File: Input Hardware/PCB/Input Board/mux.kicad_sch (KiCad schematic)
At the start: 4 parts

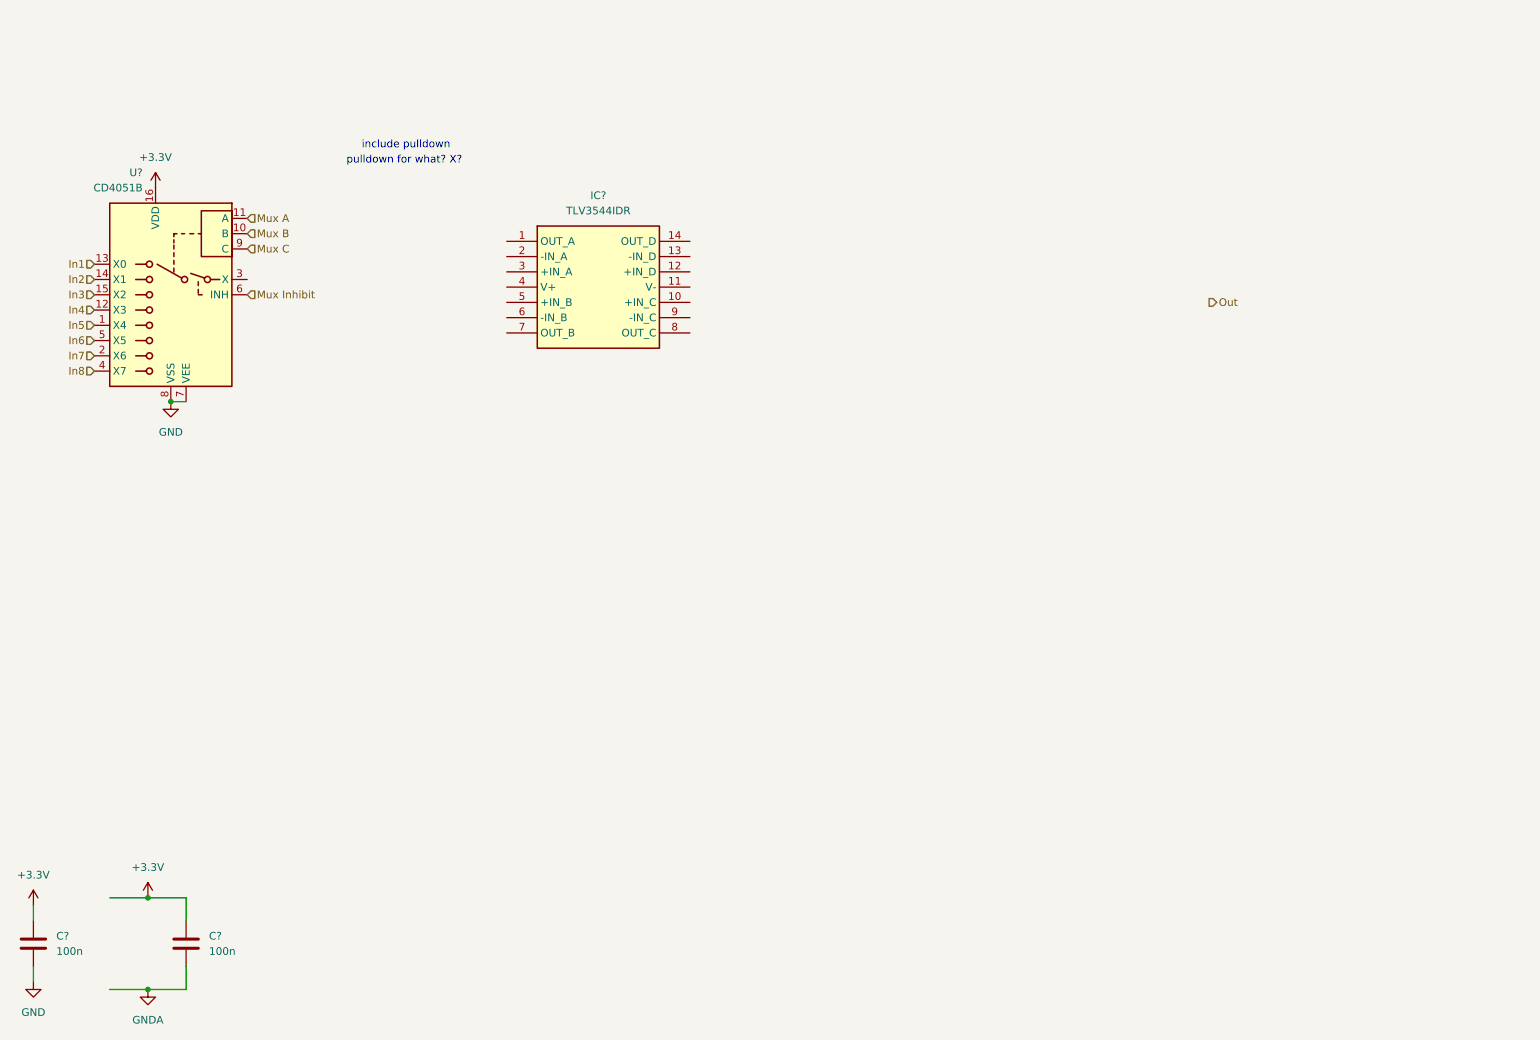
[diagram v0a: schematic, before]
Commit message: opamp symbol
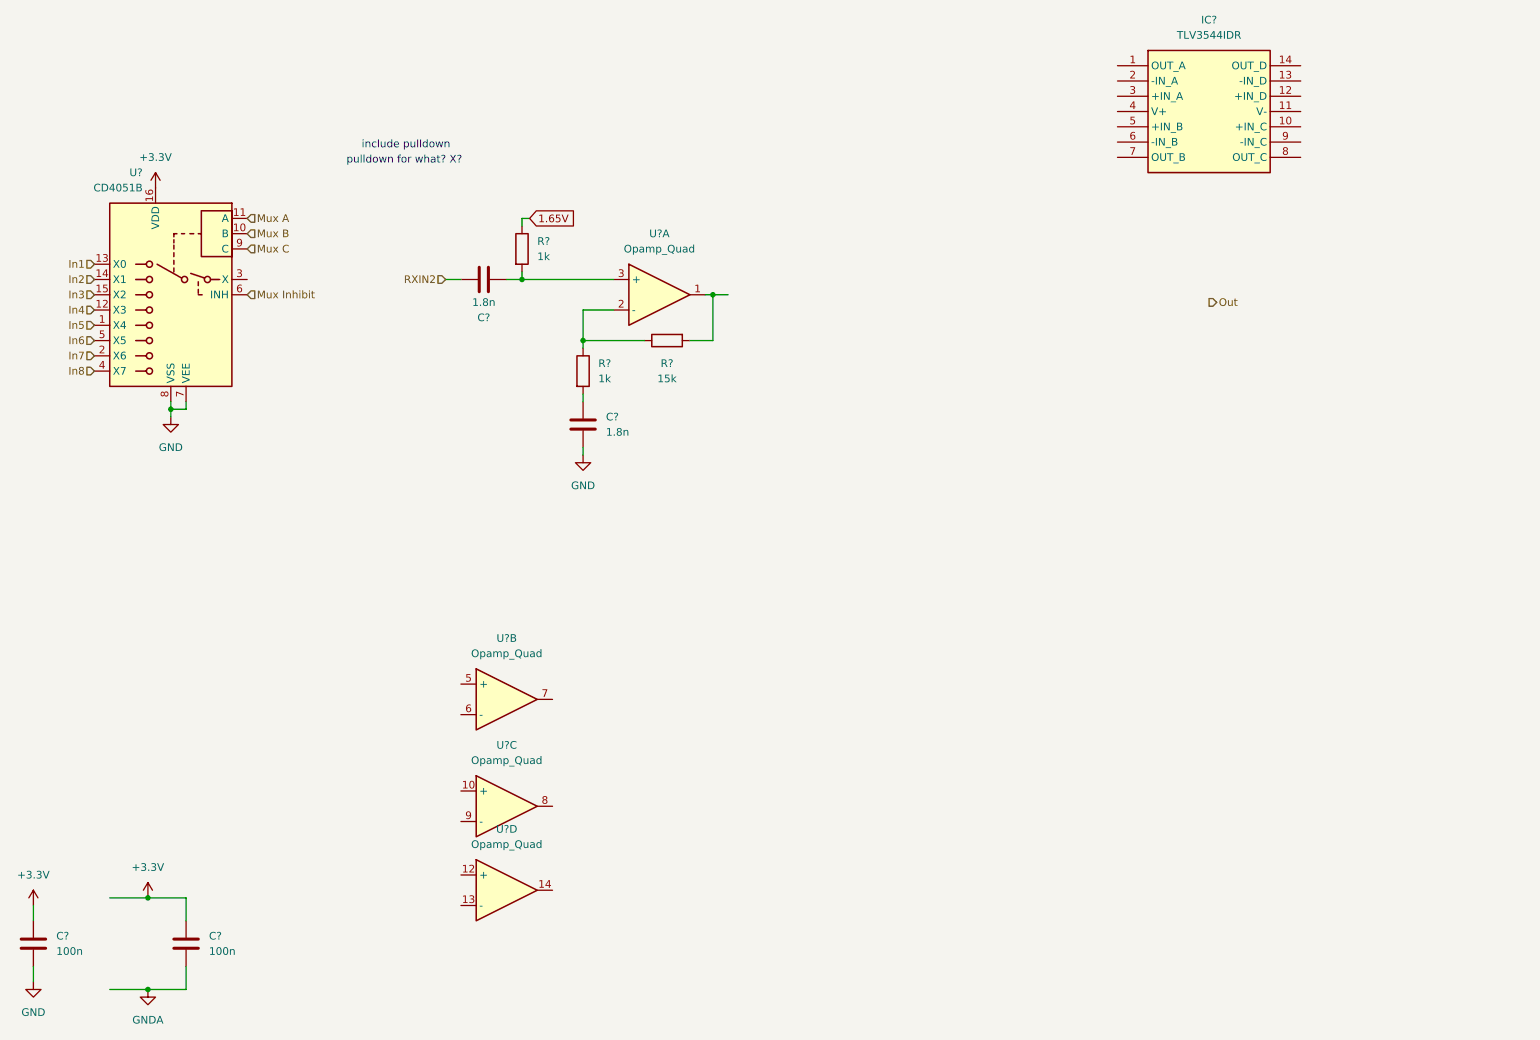
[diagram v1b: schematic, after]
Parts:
- added C? (x2): 1.8n, Capacitor_SMD:C_0603_1608Metric, symbol Device:C
- added R? (x2): 1k, Resistor_SMD:R_0603_1608Metric, symbol Device:R
- added R?: 15k, Resistor_SMD:R_0603_1608Metric, symbol Device:R
- added U? (x4): Opamp_Quad, symbol Device:Opamp_Quad
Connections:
- net GND: now also C?.2
- new net: C?.1, R?.2, U?.3 (+)
- new net: R?.2, U?.1
- new net: R?.1, R?.1, U?.2 (-)
- new net: C?.1, R?.2
- new net 1.65V: R?.1
- new net RXIN2: C?.2
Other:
- moved on the sheet: IC?

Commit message: spices
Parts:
- added R?: 10k, Resistor_SMD:R_0603_1608Metric, symbol Device:R
- added U?: Opamp_Quad, symbol Device:Opamp_Quad
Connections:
- net +3.3V: now also U?.4 (V+)
- net GND: now also R?.2
- net GNDA: now also U?.11 (V-)
- net Mux Inhibit: now also R?.1
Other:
- note removed: "include pulldown"
- note removed: "pulldown for what? X?"
- moved on the sheet: C?, U?B, U?C, U?D

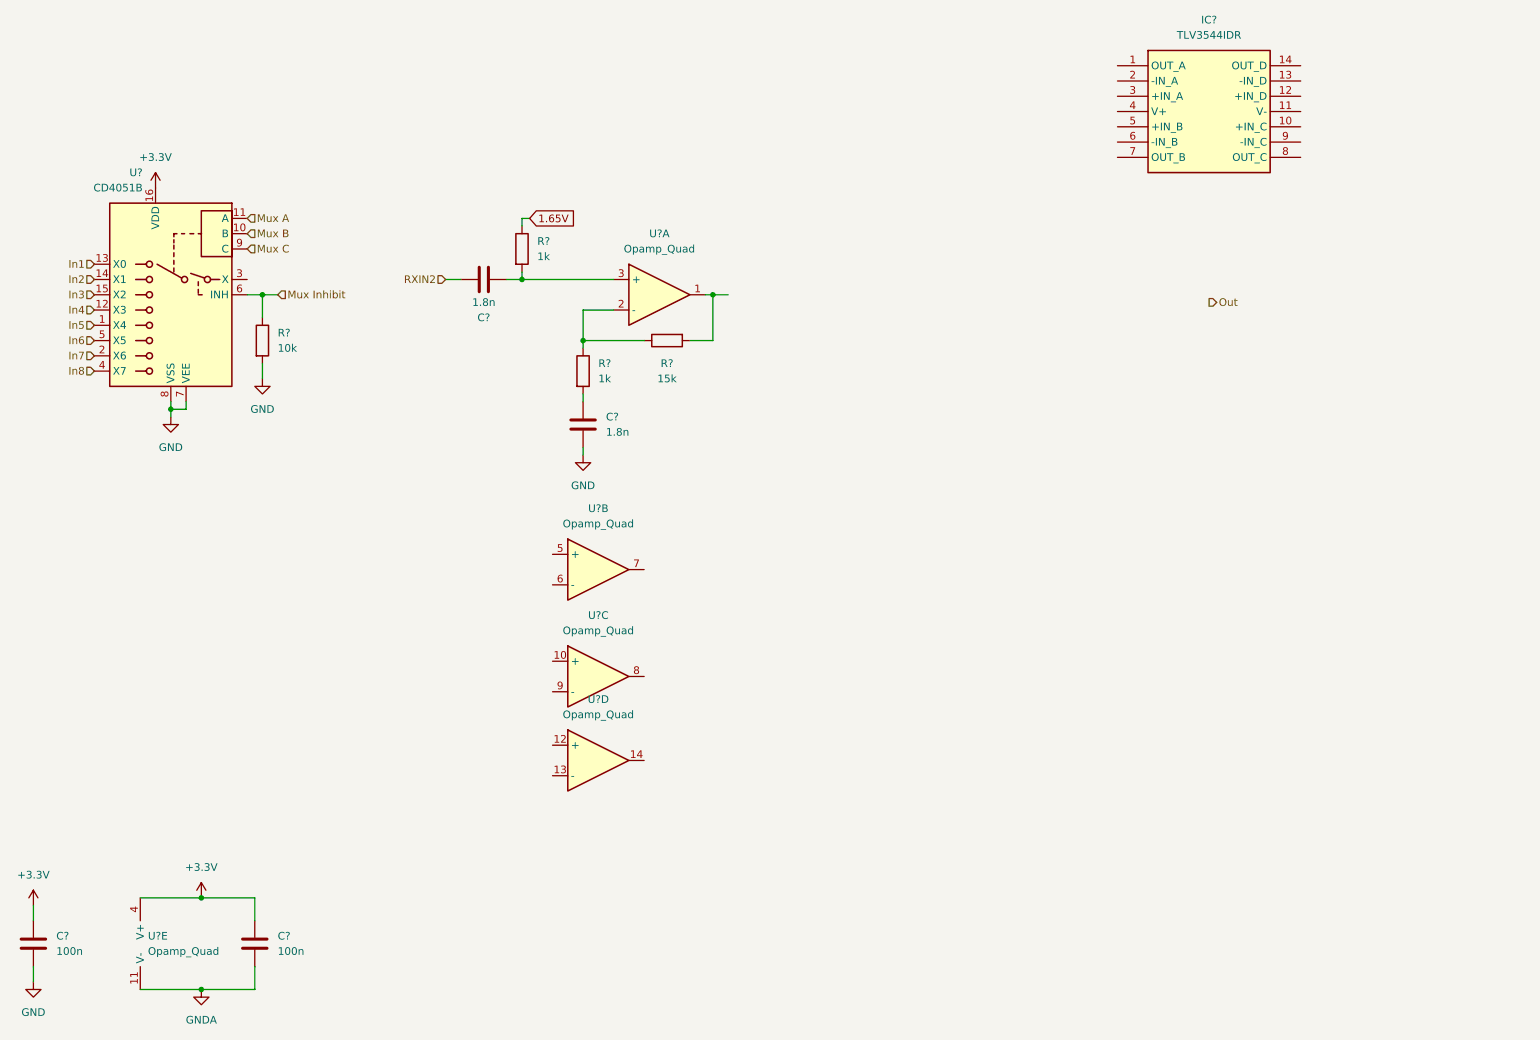
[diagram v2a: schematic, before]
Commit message: adc bandpass amp and rootpage update
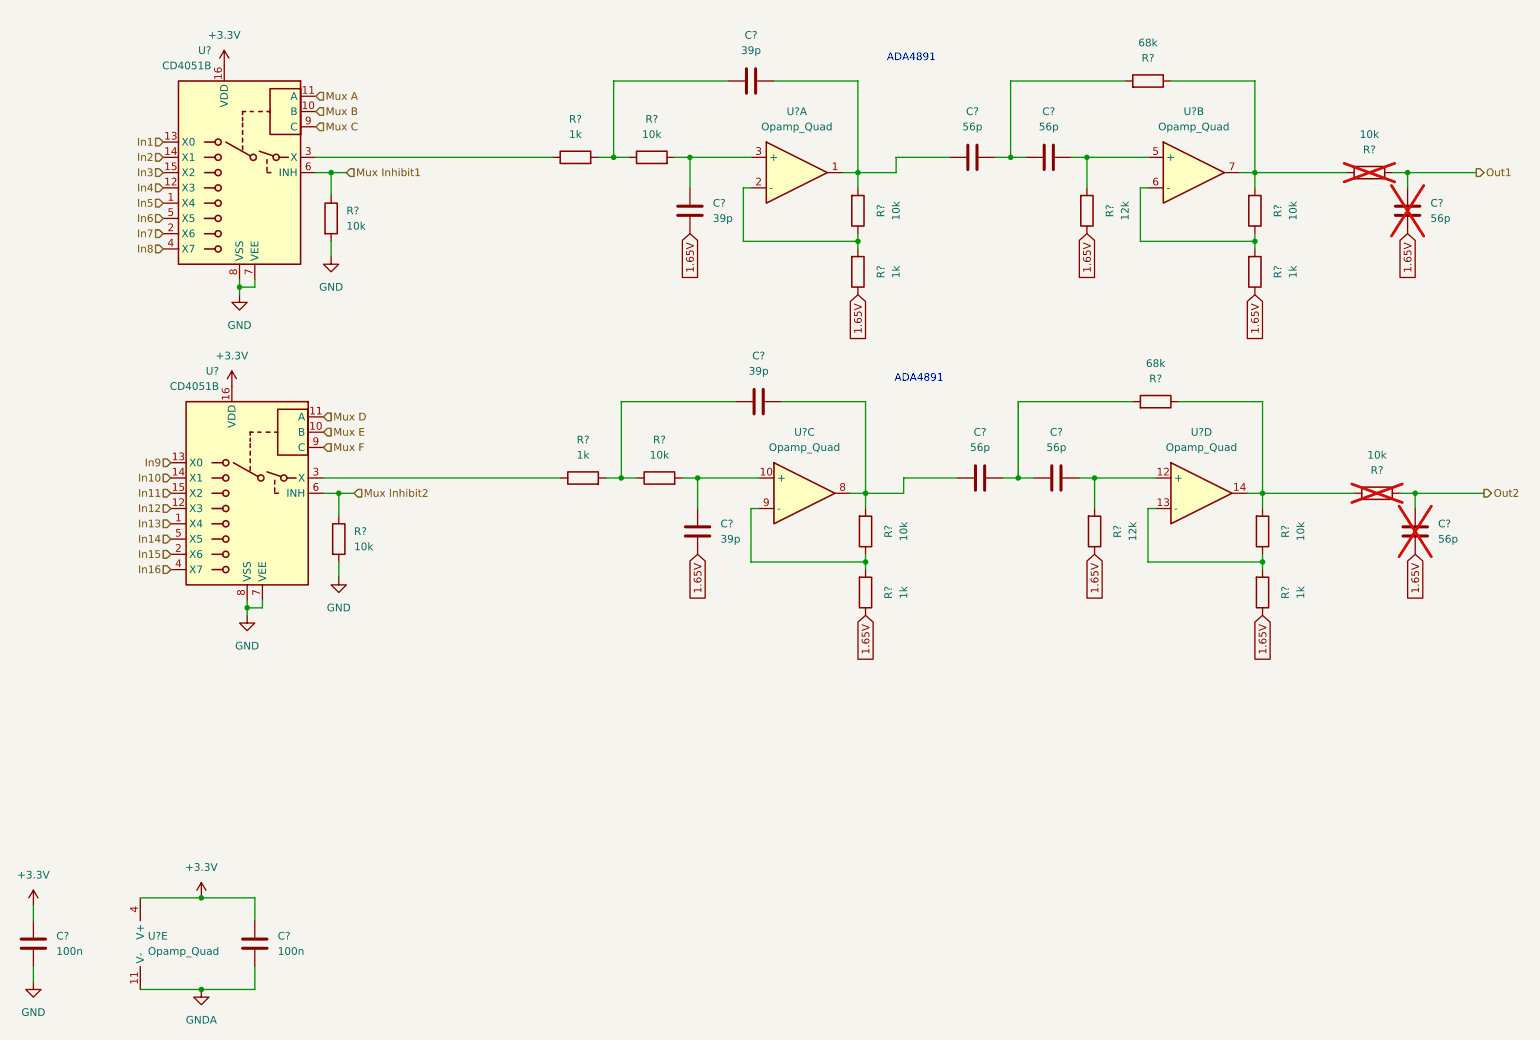
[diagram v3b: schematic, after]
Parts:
- removed C? (x2): 1.8n, Capacitor_SMD:C_0603_1608Metric, symbol Device:C
- removed IC?: TLV3544IDR, SOIC127P600X175-14N, symbol TLV3544IDR:TLV3544IDR
- removed R? (x2): 1k, Resistor_SMD:R_0603_1608Metric, symbol Device:R
- removed R?: 15k, Resistor_SMD:R_0603_1608Metric, symbol Device:R
- removed U? (x3): Opamp_Quad, symbol Device:Opamp_Quad
- added C? (x6): 56p, symbol Device:C
- added C? (x4): 39p, symbol Device:C
- added R? (x9): 10k, Resistor_SMD:R_0603_1608Metric, symbol Device:R
- added R? (x6): 1k, Resistor_SMD:R_0603_1608Metric, symbol Device:R
- added R? (x2): 68k, Resistor_SMD:R_0603_1608Metric, symbol Device:R
- added R? (x2): 12k, Resistor_SMD:R_0603_1608Metric, symbol Device:R
- added U? (x3): Opamp_Quad, symbol Device:Opamp_Quad
- added U?: CD4051B, symbol Analog_Switch:CD4051B
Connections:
- net +3.3V: now also U?.16 (VDD)
- net 1.65V: now also C?.1, C?.1, C?.2, C?.2, R?.1, R?.1, R?.1, R?.1, R?.1, R?.1
- net GND: now also R?.2, U?.7 (VEE), U?.8 (VSS)
- net at U?.3 (+): now also C?.1, R?.2
- net at U?.1: now also C?.1, C?.2, R?.2
- net at U?.2 (-): now also R?.1, R?.2
- net at U?.3 (X): now also R?.1
- net Mux Inhibit renamed Mux Inhibit1
- new net: R?.1, R?.2, U?.13 (-)
- new net: R?.1, R?.2, R?.2, U?.14
- new net: C?.1, C?.2, R?.2 (x2)
- new net: C?.2, R?.2, U?.12 (+)
- new net: R?.1, R?.2, U?.9 (-)
- new net: C?.1, R?.1, R?.2 (x2)
- new net: C?.1, C?.2, R?.2, U?.8
- new net: C?.2, R?.2, U?.5 (+)
- new net: R?.1, U?.3 (X)
- new net: R?.1, R?.2, U?.6 (-)
- new net: R?.1, R?.2, R?.2, U?.7
- new net: C?.1, R?.2, U?.10 (+)
- new net In10: U?.14 (X1)
- new net In11: U?.15 (X2)
- new net In12: U?.12 (X3)
- new net In13: U?.1 (X4)
- new net In14: U?.5 (X5)
- new net In15: U?.2 (X6)
- new net In16: U?.4 (X7)
- new net In9: U?.13 (X0)
- new net Mux D: U?.11 (A)
- new net Mux E: U?.10 (B)
- new net Mux F: U?.9 (C)
- new net Mux Inhibit2: R?.1, U?.6 (INH)
- new net Out1: C?.2, R?.1
- new net Out2: C?.2, R?.1
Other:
- note added: "ADA4891"
- moved on the sheet: R?, U?, U?A

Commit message: help
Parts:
- removed R? (x2): 10k, Resistor_SMD:R_0603_1608Metric, symbol Device:R
- added C?: 100n, Capacitor_SMD:C_0603_1608Metric, symbol Device:C
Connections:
- net Mux Inhibit2 is gone; now on net Mux Inhibit: U?.6 (INH)
- net +3.3V: now also C?.1
- net GND: now also C?.2
- net Mux Inhibit1 renamed Mux Inhibit
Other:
- moved on the sheet: C?, U?E
